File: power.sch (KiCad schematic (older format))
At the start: 22 parts, among them SW5 SW_DPST_NKK_M2021, U13 LM317_SOT223_4pin, U14 LM317_SOT223_4pin

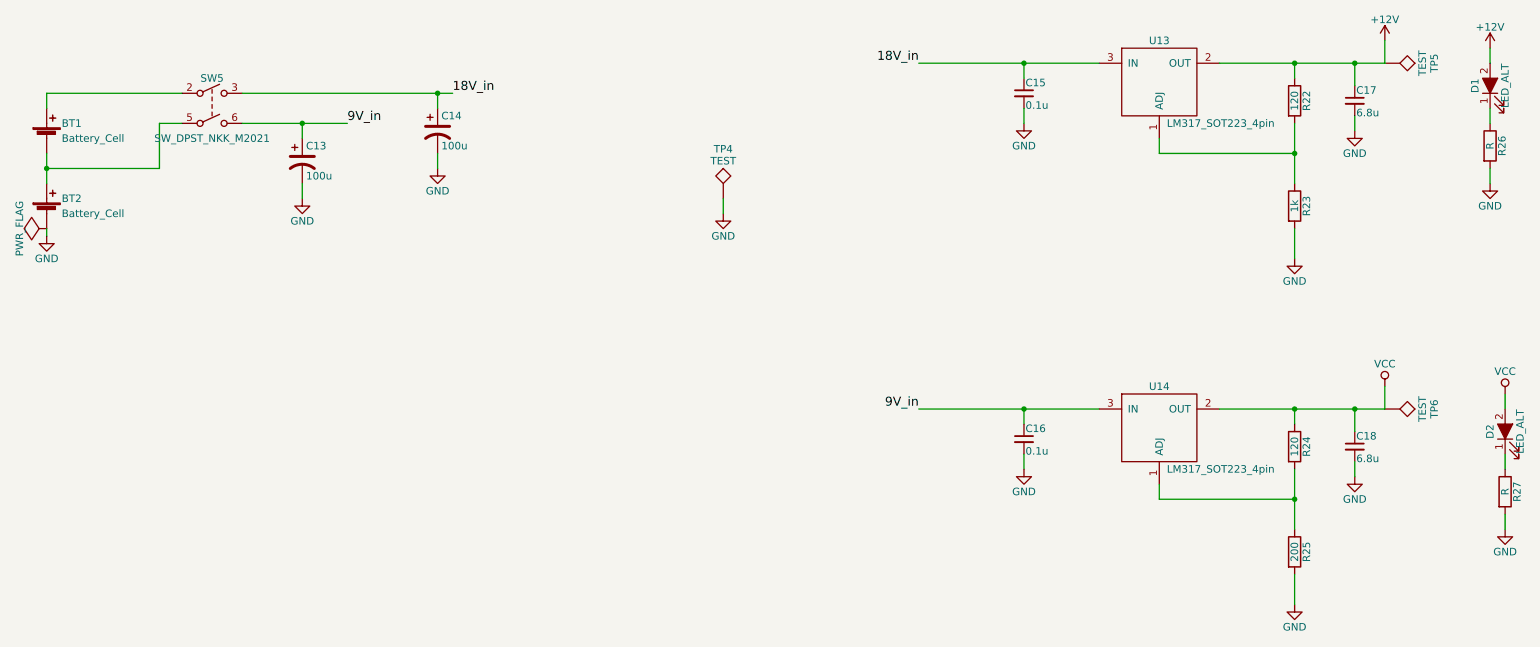
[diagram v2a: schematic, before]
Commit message: R2 PCB rotary switches closer to middle of board
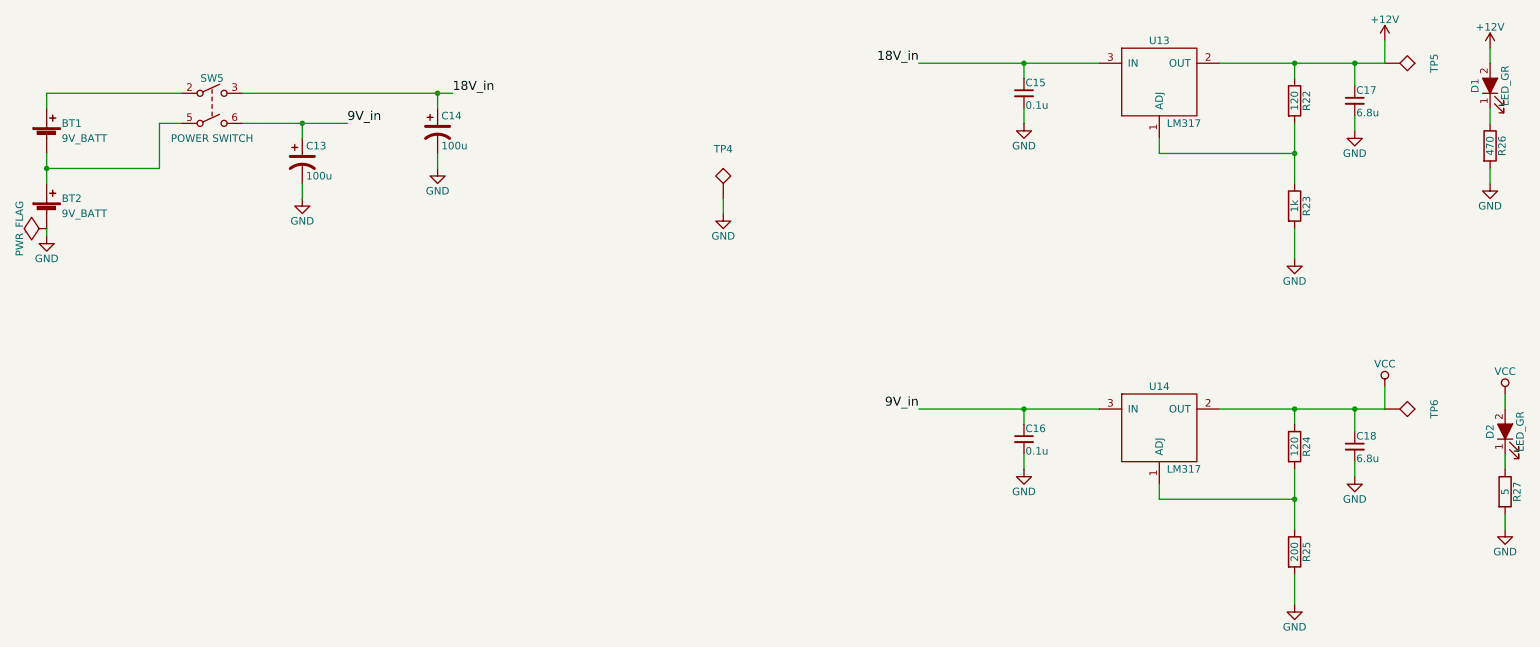
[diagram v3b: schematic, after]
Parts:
- BT1, BT2: value Battery_Cell -> 9V_BATT
- C13, C14: Distributor (none) -> Mouser; Distributor PN (none) -> 647-URS1E101MDD; Manufacturer (none) -> Nichicon; Manufacturer PN (none) -> URS1E101MDD; URL (none) -> http://www.mouser.com/Search/ProductDetail.aspx?R=URS1E101M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; Unit Price (none) -> 0.34
- D1, D2: value LED_ALT -> LED_GR; Distributor (none) -> Mouser; Distributor PN (none) -> 941-C503BGCNCY0C0792; Manufacturer (none) -> Cree; Manufacturer PN (none) -> C503B-GCN-CY0C0792; URL (none) -> http://www.mouser.com/Search/ProductDetail.aspx?R=C503B-GCN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; Unit Price (none) -> 0.24
- R26: value R -> 470
- R27: value R -> 5
- SW5: value SW_DPST_NKK_M2021 -> POWER SWITCH; Distributor (none) -> Mouser; Distributor PN (none) -> 633-M2021SS1W03; Manufacturer (none) -> NKK; Manufacturer PN (none) -> M2021SS1W03; URL (none) -> http://www.mouser.com/Search/ProductDetail.aspx?R=M2021SS1W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; Unit Price (none) -> 4.32
- TP4: value TEST -> GND
- TP5: value TEST -> 12V
- TP6: value TEST -> 3.3V
- U13, U14: value LM317_SOT223_4pin -> LM317; Distributor (none) -> Mouser; Distributor PN (none) -> 595-LM317DCYR; Manufacturer (none) -> TI; Manufacturer PN (none) -> LM317DCYR; URL (none) -> http://www.mouser.com/Search/ProductDetail.aspx?R=LM317DCYR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; Unit Price (none) -> 0.74

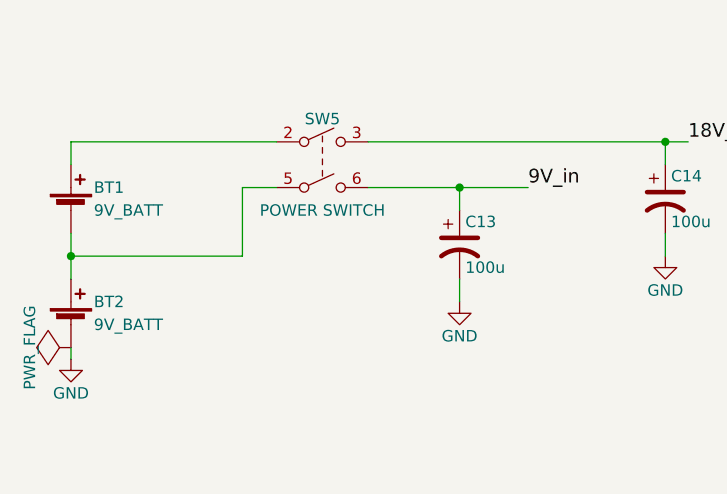
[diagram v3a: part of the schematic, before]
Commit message: update switch models in library, rotate final clock division switch
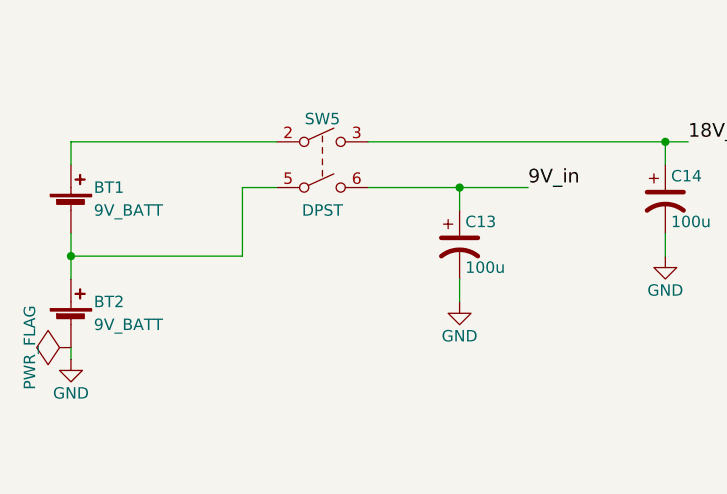
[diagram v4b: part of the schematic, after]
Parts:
- SW5: value POWER SWITCH -> DPST
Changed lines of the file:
@@
 P 2100 1700
 F 0 "SW5" H 2100 1900 50  0000 C CNN
-F 1 "POWER SWITCH" H 2100 1500 50  0000 C CNN
+F 1 "DPST" H 2100 1500 50  0000 C CNN
 F 2 "calbox:SW_NKK_M20xxxxx03_DPST" H 2100 1700 50  0001 C CNN
 F 3 "http://www.mouser.com/ds/2/295/MtogglesBushing-31423.pdf" H 2100 1700 50  0001 C CNN

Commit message: Several schematic & layout changes after building first boards
- increase current limiting resistors on LEDs to make them less blinding
- add speedup cap, increase base resistor on voltage output switching
  transistor for better high frequency performance (should work up to 10MHz)
- change switched/constant voltage output toggle switch to actually work
  (now toggles between switched voltage output and constant voltage
  output, rather than switched and 0V output)
- add inverter to make div-by-5 circuit work
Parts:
- R25: value 200 -> 196
- R27: value 5 -> 5.1
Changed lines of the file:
@@
 	1000 2000 1000 2200
 $Comp
-L GND #PWR069
+L GND #PWR071
 U 1 1 58C4B1BE
 P 1000 2550
-F 0 "#PWR069" H 1000 2300 50  0001 C CNN
+F 0 "#PWR071" H 1000 2300 50  0001 C CNN
 F 1 "GND" H 1000 2400 50  0000 C CNN
 F 2 "" H 1000 2550 50  0000 C CNN
@@
 P 9300 4650
 F 0 "R25" V 9380 4650 50  0000 C CNN
-F 1 "200" V 9300 4650 50  0000 C CNN
+F 1 "196" V 9300 4650 50  0000 C CNN
 F 2 "Resistors_SMD:R_0805_HandSoldering" V 9230 4650 50  0001 C CNN
 F 3 "" H 9300 4650 50  0000 C CNN
@@
 Connection ~ 9300 4300
 $Comp
-L GND #PWR070
+L GND #PWR072
 U 1 1 58C50174
 P 9300 5000
-F 0 "#PWR070" H 9300 4750 50  0001 C CNN
+F 0 "#PWR072" H 9300 4750 50  0001 C CNN
 F 1 "GND" H 9300 4850 50  0000 C CNN
 F 2 "" H 9300 5000 50  0000 C CNN
@@
 $EndComp
 $Comp
-L GND #PWR071
+L GND #PWR073
 U 1 1 58C505E0
 P 7500 4100
-F 0 "#PWR071" H 7500 3850 50  0001 C CNN
+F 0 "#PWR073" H 7500 3850 50  0001 C CNN
 F 1 "GND" H 7500 3950 50  0000 C CNN
 F 2 "" H 7500 4100 50  0000 C CNN
@@
 Connection ~ 7500 3700
 $Comp
-L VCC #PWR072
+L VCC #PWR074
 U 1 1 58C5068E
 P 9900 3550
-F 0 "#PWR072" H 9900 3400 50  0001 C CNN
+F 0 "#PWR074" H 9900 3400 50  0001 C CNN
 F 1 "VCC" H 9900 3700 50  0000 C CNN
 F 2 "" H 9900 3550 50  0000 C CNN
@@
 Connection ~ 9300 3700
 $Comp
-L GND #PWR073
+L GND #PWR075
 U 1 1 58C50749
 P 9700 4150
-F 0 "#PWR073" H 9700 3900 50  0001 C CNN
+F 0 "#PWR075" H 9700 3900 50  0001 C CNN
 F 1 "GND" H 9700 4000 50  0000 C CNN
 F 2 "" H 9700 4150 50  0000 C CNN
@@
 Connection ~ 9300 2000
 $Comp
-L GND #PWR074
+L GND #PWR076
 U 1 1 58C7F4E2
 P 9300 2700
-F 0 "#PWR074" H 9300 2450 50  0001 C CNN
+F 0 "#PWR076" H 9300 2450 50  0001 C CNN
 F 1 "GND" H 9300 2550 50  0000 C CNN
 F 2 "" H 9300 2700 50  0000 C CNN
@@
 $EndComp
 $Comp
-L GND #PWR075
+L GND #PWR077
 U 1 1 58C7F4EF
 P 7500 1800
-F 0 "#PWR075" H 7500 1550 50  0001 C CNN
+F 0 "#PWR077" H 7500 1550 50  0001 C CNN
 F 1 "GND" H 7500 1650 50  0000 C CNN
 F 2 "" H 7500 1800 50  0000 C CNN
@@
 Connection ~ 9300 1400
 $Comp
-L GND #PWR076
+L GND #PWR078
 U 1 1 58C7F506
 P 9700 1850
-F 0 "#PWR076" H 9700 1600 50  0001 C CNN
+F 0 "#PWR078" H 9700 1600 50  0001 C CNN
 F 1 "GND" H 9700 1700 50  0000 C CNN
 F 2 "" H 9700 1850 50  0000 C CNN
@@
 18V_in
 $Comp
-L +12V #PWR077
+L +12V #PWR079
 U 1 1 58C7F582
 P 9900 1250
-F 0 "#PWR077" H 9900 1100 50  0001 C CNN
+F 0 "#PWR079" H 9900 1100 50  0001 C CNN
 F 1 "+12V" H 9900 1390 50  0000 C CNN
 F 2 "" H 9900 1250 50  0000 C CNN
@@
 $EndComp
 $Comp
-L GND #PWR078
+L GND #PWR080
 U 1 1 58C7FF7B
 P 2700 2300
-F 0 "#PWR078" H 2700 2050 50  0001 C CNN
+F 0 "#PWR080" H 2700 2050 50  0001 C CNN
 F 1 "GND" H 2700 2150 50  0000 C CNN
 F 2 "" H 2700 2300 50  0000 C CNN
@@
 $EndComp
 $Comp
-L GND #PWR079
+L GND #PWR081
 U 1 1 58C7FFBA
 P 3600 2100
-F 0 "#PWR079" H 3600 1850 50  0001 C CNN
+F 0 "#PWR081" H 3600 1850 50  0001 C CNN
 F 1 "GND" H 3600 1950 50  0000 C CNN
 F 2 "" H 3600 2100 50  0000 C CNN
@@
 	2700 2300 2700 2200
 $Comp
-L PWR_FLAG #FLG080
+L PWR_FLAG #FLG082
 U 1 1 58C81A82
 P 1000 2500
-F 0 "#FLG080" H 1000 2595 50  0001 C CNN
+F 0 "#FLG082" H 1000 2595 50  0001 C CNN
 F 1 "PWR_FLAG" H 1000 2680 50  0000 C CNN
 F 2 "" H 1000 2500 50  0000 C CNN
@@
 P 10700 4250
 F 0 "R27" V 10780 4250 50  0000 C CNN
-F 1 "5" V 10700 4250 50  0000 C CNN
+F 1 "5.1" V 10700 4250 50  0000 C CNN
 F 2 "Resistors_SMD:R_0805_HandSoldering" V 10630 4250 50  0001 C CNN
 F 3 "" H 10700 4250 50  0000 C CNN
@@
 	10600 1700 10600 1800
 $Comp
-L GND #PWR081
+L GND #PWR083
 U 1 1 58C85746
 P 10600 2200
-F 0 "#PWR081" H 10600 1950 50  0001 C CNN
+F 0 "#PWR083" H 10600 1950 50  0001 C CNN
 F 1 "GND" H 10600 2050 50  0000 C CNN
 F 2 "" H 10600 2200 50  0000 C CNN
@@
 	10600 2100 10600 2200
 $Comp
-L +12V #PWR082
+L +12V #PWR084
 U 1 1 58C857D7
 P 10600 1300
-F 0 "#PWR082" H 10600 1150 50  0001 C CNN
+F 0 "#PWR084" H 10600 1150 50  0001 C CNN
 F 1 "+12V" H 10600 1440 50  0000 C CNN
 F 2 "" H 10600 1300 50  0000 C CNN
@@
 	10600 1300 10600 1400
 $Comp
-L GND #PWR083
+L GND #PWR085
 U 1 1 58C85A19
 P 10700 4500
-F 0 "#PWR083" H 10700 4250 50  0001 C CNN
+F 0 "#PWR085" H 10700 4250 50  0001 C CNN
 F 1 "GND" H 10700 4350 50  0000 C CNN
 F 2 "" H 10700 4500 50  0000 C CNN
@@
 	10700 4000 10700 4100
 $Comp
-L VCC #PWR084
+L VCC #PWR086
 U 1 1 58C85C4B
 P 10700 3600
-F 0 "#PWR084" H 10700 3450 50  0001 C CNN
+F 0 "#PWR086" H 10700 3450 50  0001 C CNN
 F 1 "VCC" H 10700 3750 50  0000 C CNN
 F 2 "" H 10700 3600 50  0000 C CNN
@@
 $EndComp
 $Comp
-L GND #PWR085
+L GND #PWR087
 U 1 1 58CA00F3
 P 5500 2400
-F 0 "#PWR085" H 5500 2150 50  0001 C CNN
+F 0 "#PWR087" H 5500 2150 50  0001 C CNN
 F 1 "GND" H 5500 2250 50  0000 C CNN
 F 2 "" H 5500 2400 50  0000 C CNN

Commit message: Update schematic for rev1
- add battery snap footprint
- add speedup cap for voltage output transistor
- correct voltage output toggle switch operation (vcc -> gnd for
  constant voltage output)
- add single gate inverter for correct divide-by-10 operation
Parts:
- BT1, BT2: footprint Pin_Headers:Pin_Header_Straight_1x02 -> calbox:battery_snap
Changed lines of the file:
@@
 Sheet 6 6
 Title "calbox power supply"
-Date ""
-Rev ""
+Date "2017-05-22"
+Rev "1"
 Comp ""
 Comment1 ""
@@
 F 0 "BT1" H 1100 2000 50  0000 L CNN
 F 1 "9V_BATT" H 1100 1900 50  0000 L CNN
-F 2 "Pin_Headers:Pin_Header_Straight_1x02" V 1000 1960 50  0001 C CNN
+F 2 "calbox:battery_snap" V 1000 1960 50  0001 C CNN
 F 3 "" V 1000 1960 50  0000 C CNN
 	1    1000 1900
@@
 F 0 "BT2" H 1100 2500 50  0000 L CNN
 F 1 "9V_BATT" H 1100 2400 50  0000 L CNN
-F 2 "Pin_Headers:Pin_Header_Straight_1x02" V 1000 2460 50  0001 C CNN
+F 2 "calbox:battery_snap" V 1000 2460 50  0001 C CNN
 F 3 "" V 1000 2460 50  0000 C CNN
 	1    1000 2400
